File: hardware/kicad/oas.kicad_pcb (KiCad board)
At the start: 2 copper layers, 120 x 103.5 mm, 69 parts, among them J1 Phoenix_MSTBA_2,5/3-G-5,08 (2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, J10 Native-USB recovery (DNP), J2 UART/Boot Recovery (DNP), J3 JST SM06B-GHS-TB (SEN66 conne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, J4 1x5 P1.27mm header (HLK-LD241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, J5 ESP32 row A (pins 1..15, ante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, J6 ESP32 row B (pins 16..30, USB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, J7 MIKROE mikroBUS pins 1..8 (AN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, J8 MIKROE mikroBUS pins 9..16 (P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, J9 JST SM04B-SRSS-TB (Qwiic / St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, Q1 AO3401A, SW1 C&K PTS645VK392LFS, U1 LM2596S-5.0, U2 TPS62933

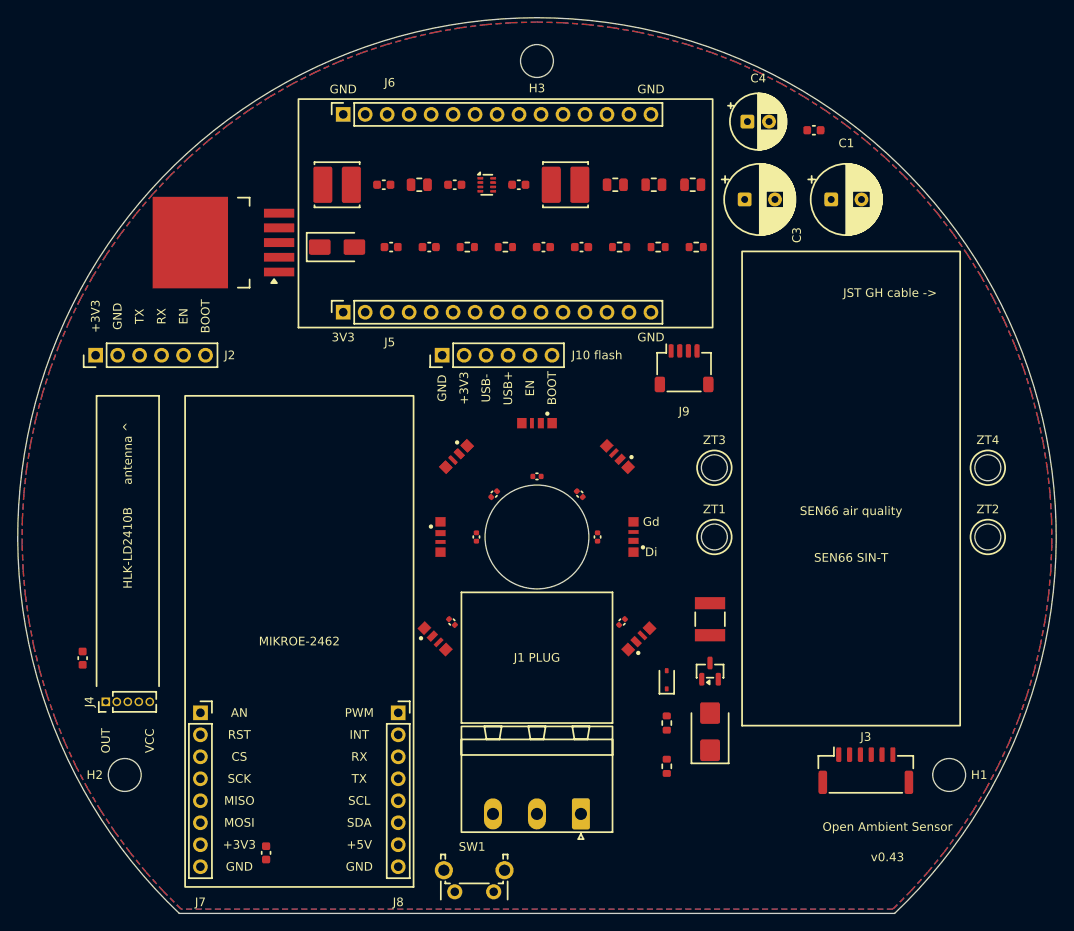
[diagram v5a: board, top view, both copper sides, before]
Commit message: feat(routing): v0.50 routing complete — full 89/89 + hand-stitched GND
The board is fully routed and DRC-clean. ROUTING_CHUNKS = ("gnd",
"autoroute"); build.py 30/30 PASS; DRC 0 violations / 0 unconnected pads.

The checkpoint snapshot (53e4ea9, 405 seg + 22 via) was stale — extracted
against a pre-Task-3 buck placement, it shorted the buck section on replay
(87 DRC violations). Re-routed from scratch:

- Freerouting 2.2.4 (Docker eclipse-temurin:25-jre) on the current
  committed placement, DSN patched to JLCDFM-strict rules (clearance
  0.20 mm, via 0.70/0.30 mm) — full 89/89 coverage, 0 unrouted nets.
- SES imported; the F.Cu GND pour (fragmented into ~19 islands by KiCad's
  zone-fill around the 89 signal nets) hand-stitched in KiCad: stitching
  vias + short GND tracks reconnecting every fragment to the continuous
  B.Cu pour.
- 3 mechanical fixes: a GND via nudged off the central-hole edge
  (0.169 -> 0.45 mm clearance); 2 co-located duplicate vias removed.

Final snapshot oas_routes.py = 613 segments + 44 vias.
pipeline/generic/03_drc.py EXPECTED_UNCONNECTED 89 -> 0 (fully routed;
any non-zero count is now a routing regression).

Co-Authored-By: Claude Opus 4.7 (1M context) <noreply@anthropic.com>
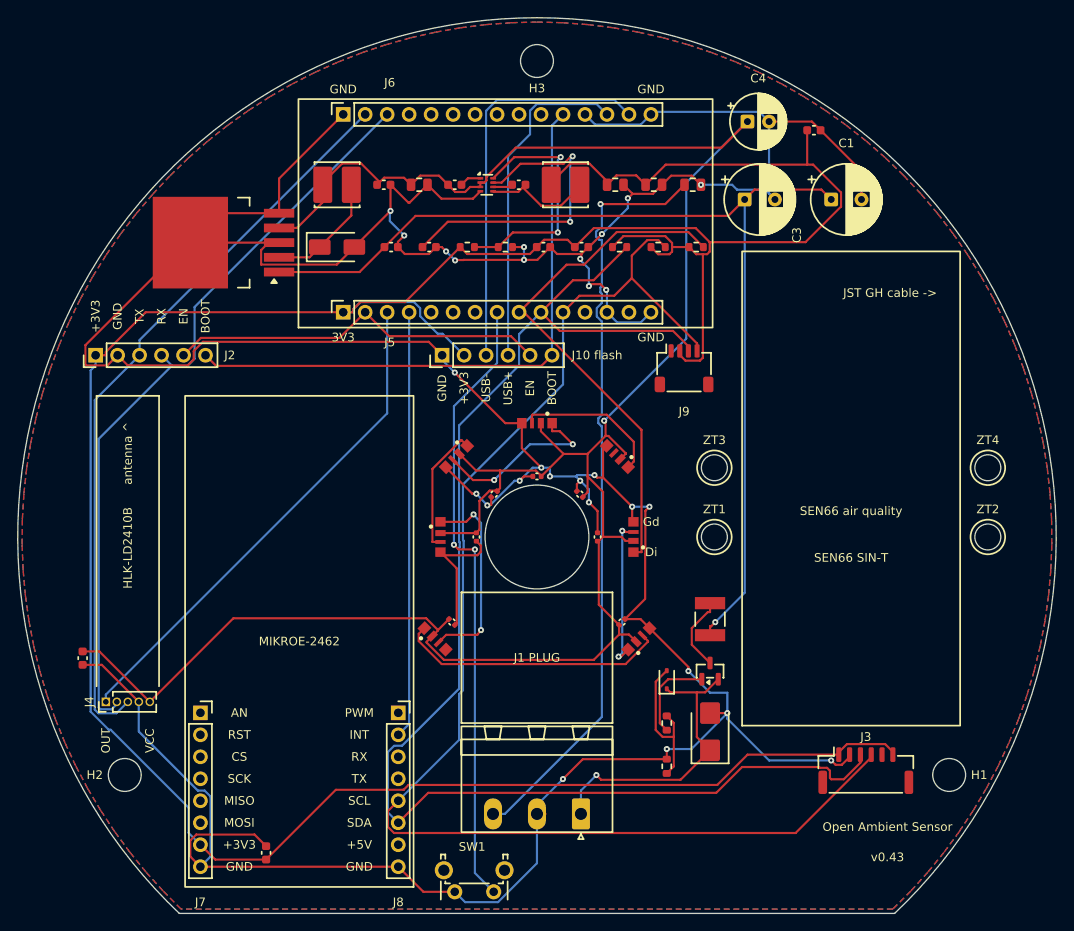
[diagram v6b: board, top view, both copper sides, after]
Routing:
- net GND: track 0.00 -> 521.7 mm, vias 0 -> 28
- net +3V3: track 0.00 -> 341.1 mm
- net +5V: track 0.00 -> 258.2 mm, vias 0 -> 1
- net /IO/I2C_SDA: track 0.00 -> 158.5 mm
- net /IO/I2C_SCL: track 0.00 -> 156.7 mm
- net +24V: track 0.00 -> 120.3 mm, vias 0 -> 1
- net Earth_Protective: track 0.00 -> 89.0 mm, vias 0 -> 1
- net /MCU/UART_RX: track 0.00 -> 87.8 mm
- net /MCU/UART_TX: track 0.00 -> 86.3 mm
- net /IO/BTN: track 0.00 -> 72.0 mm, vias 0 -> 2
- net /IO/BOOT: track 0.00 -> 69.4 mm
- net /MCU/WS2812_DIN: track 0.00 -> 60.7 mm
- net /MCU/LD2410_OUT: track 0.00 -> 58.5 mm
- net /MCU/NFC_FD: track 0.00 -> 49.4 mm
- net /IO/USB_DM: track 0.00 -> 46.0 mm
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
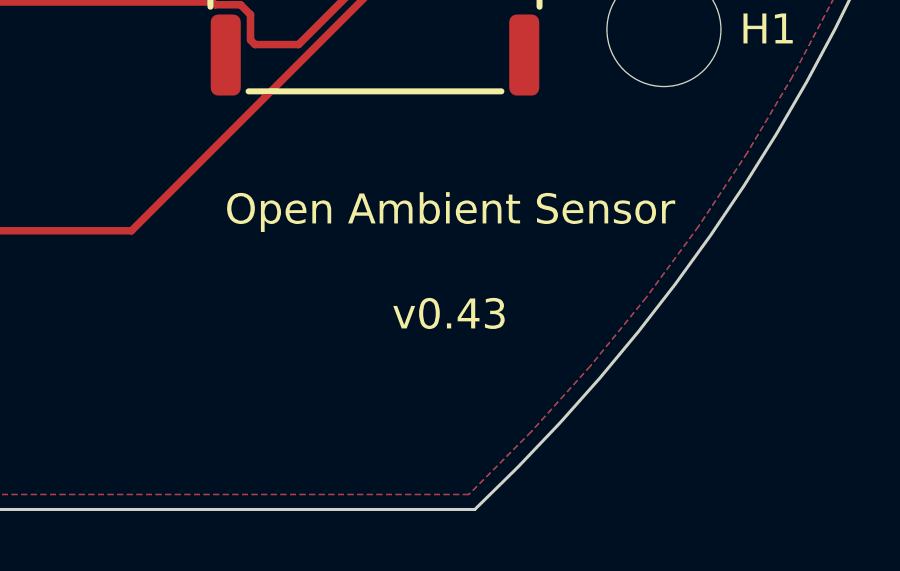
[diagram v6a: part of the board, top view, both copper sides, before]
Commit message: chore(version): bump board silkscreen version v0.43 -> v0.50
OAS_VERSION_LINE (boardgen/_common.py) drives the F.SilkS version label
in the SE pocket under J3 — single source of truth for the on-board
version stamp. Bumped to v0.50 to match the completed routing rework.
build.py 30/30 PASS.

Co-Authored-By: Claude Opus 4.7 (1M context) <noreply@anthropic.com>
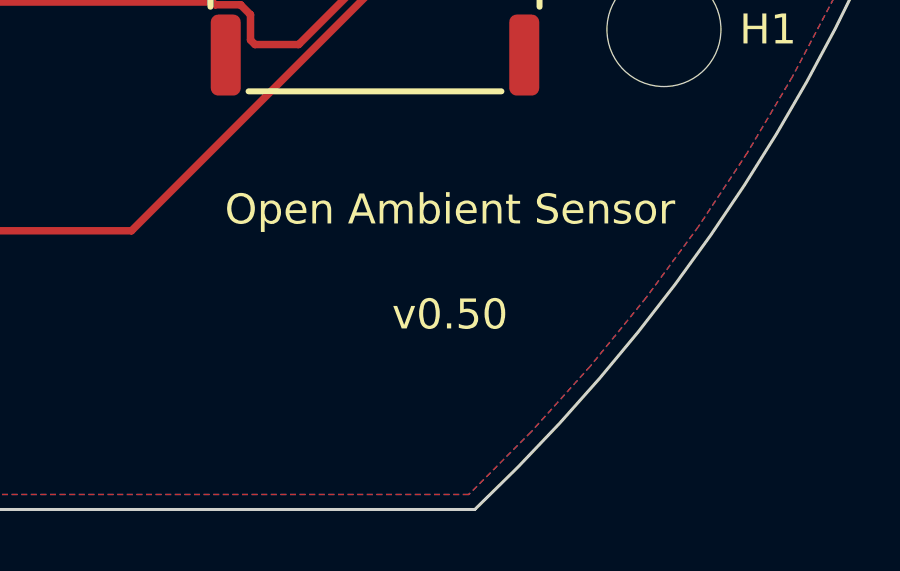
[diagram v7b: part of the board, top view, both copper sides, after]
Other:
- board text added: "v0.50"
- board text removed: "v0.43"
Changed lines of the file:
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@@
 	)
 )
-(gr_text "v0.43"
+(gr_text "v0.50"
 	(at 189 142 0)
 	(layer "F.SilkS")

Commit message: fix(dfm): shrink central hole Ø12->Ø10 + drop via-in-pad on C2
Two JLCDFM fixes (build.py 30/30 PASS, DRC 0 violations / 0 unconnected):

- Central cable hole Ø12 -> Ø10 (CABLE_HOLE_DIAMETER). The 5 LED-ring
  decoupling caps C20/C24/C25/C26/C27 (cap radius 7.0 mm) sat 0.75 mm
  from the Ø12 hole edge -> JLCDFM "Component to board edge distance"
  (5 Warning). Ø10 lifts that to ~1.7 mm. The 3x1.5 mm2 supply cable
  (YDY 3x1.5, Ø8-9 mm) still passes. No component or track moved -
  shrinking the hole was chosen over moving the caps precisely so the
  committed routing stays intact.

- Removed GND via:0031 - it sat dead-centre on C2 pad 2 (via-in-pad),
  tripping JLCDFM "Lead to hole distance" (0 mm Danger) and "Silkscreen
  to hole" (0 mm Danger). C2 pad 2 (GND) stays connected through the
  GND pour - DRC confirms 0 unconnected.

Co-Authored-By: Claude Opus 4.7 (1M context) <noreply@anthropic.com>
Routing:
- net GND: vias 28 -> 27
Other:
- outline, holes or cut-outs redrawn
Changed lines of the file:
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@@
 (gr_circle
 	(center 148.5 105)
-	(end 154.5 105)
+	(end 153.5 105)
 	(stroke (width 0.1) (type solid))
 	(fill no)
@@
 		(size 0.7)
 		(drill 0.3)
-		(layers "F.Cu" "B.Cu")
-		(net 17)
-	)
-	(via
-		(at 167.45 64.3)
-		(size 0.7)
-		(drill 0.3)
